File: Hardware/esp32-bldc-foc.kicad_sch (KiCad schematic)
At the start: 39 parts, among them J1 ENCODER, J2 I2C2, J3 VDRIVE, J4 MOTOR, P1 PCB_Pin_Breakout, P10 PCB_Pin_Breakout, P11 PCB_Pin_Breakout, P12 PCB_Pin_Breakout, P13 PCB_Pin_Breakout, P14 PCB_Pin_Breakout, P15 PCB_Pin_Breakout, P16 PCB_Pin_Breakout, P17 PCB_Pin_Breakout, P18 PCB_Pin_Breakout, P19 PCB_Pin_Breakout, P2 PCB_Pin_Breakout, P20 PCB_Pin_Breakout, P21 PCB_Pin_Breakout, P3 PCB_Pin_Breakout, P4 PCB_Pin_Breakout, P5 PCB_Pin_Breakout, P6 PCB_Pin_Breakout, P7 PCB_Pin_Breakout, P8 PCB_Pin_Breakout, P9 PCB_Pin_Breakout, U1 ESP32-S3-WROOM-1, U3 SRV05-4, U6 EG2133

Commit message: Pretty much all components now have values
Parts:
- added C16: 10u, symbol Device:C_Small
- C1: value C -> 10u
- C13, C2: value C -> 100n
- C3: value C -> 1u
- L1: value L -> BLM21
- R1, R3: value R -> 10k
- R5: value R_Small -> 10R
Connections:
- new net GND2: C16.1
- new net Vdrive: C16.2
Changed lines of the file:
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@@
 	(wire
 		(pts
+			(xy 49.53 167.64) (xy 49.53 170.18)
+		)
+		(stroke
+			(width 0)
+			(type default)
+		)
+	)
+	(wire
+		(pts
 			(xy 29.21 152.4) (xy 29.21 140.97)
 		)
@@
 	(wire
 		(pts
+			(xy 49.53 175.26) (xy 49.53 177.8)
+		)
+		(stroke
+			(width 0)
+			(type default)
+		)
+	)
+	(wire
+		(pts
 			(xy 87.63 134.62) (xy 90.17 134.62)
 		)
@@
 			)
 		)
-		(property "Value" "C"
+		(property "Value" "1u"
 			(at 232.791 138.3721 0)
 			(effects
@@
 			)
 		)
-		(property "Value" "C"
+		(property "Value" "100n"
 			(at 21.209 145.9921 0)
 			(effects
@@
 	)
 	(symbol
+		(lib_id "power:Vdrive")
+		(at 49.53 167.64 0)
+		(unit 1)
+		(exclude_from_sim no)
+		(in_bom yes)
+		(on_board yes)
+		(dnp no)
+		(fields_autoplaced yes)
+		(property "Reference" "#PWR01"
+			(at 49.53 171.45 0)
+			(effects
+				(font
+					(size 1.27 1.27)
+				)
+				(hide yes)
+			)
+		)
+		(property "Value" "Vdrive"
+			(at 49.53 163.5069 0)
+			(effects
+				(font
+					(size 1.27 1.27)
+				)
+			)
+		)
+		(property "Footprint" ""
+			(at 49.53 167.64 0)
+			(effects
+				(font
+					(size 1.27 1.27)
+				)
+				(hide yes)
+			)
+		)
+		(property "Datasheet" ""
+			(at 49.53 167.64 0)
+			(effects
+				(font
+					(size 1.27 1.27)
+				)
+				(hide yes)
+			)
+		)
+		(property "Description" "Power symbol creates a global label with name \"Vdrive\""
+			(at 49.53 167.64 0)
+			(effects
+				(font
+					(size 1.27 1.27)
+				)
+				(hide yes)
+			)
+		)
+		(pin "1"
+		)
+		(instances
+			(project "esp32-bldc-foc"
+				(path "/5fd9cc58-24f5-445f-b12c-0418263ff67c"
+					(reference "#PWR01")
+					(unit 1)
+				)
+			)
+		)
+	)
+	(symbol
 		(lib_id "power:+5V")
 		(at 168.91 125.73 0)
@@
 			)
 		)
-		(property "Value" "L"
+		(property "Value" "BLM21"
 			(at 55.2449 81.2221 0)
 			(effects
@@
 			)
 		)
-		(property "Value" "R"
+		(property "Value" "10k"
 			(at 267.208 125.6721 0)
 			(effects
@@
 			)
 		)
-		(property "Value" "R_Small"
+		(property "Value" "10R"
 			(at 56.1086 72.3321 0)
 			(effects
@@
 			)
 		)
-		(property "Value" "R"
+		(property "Value" "10k"
 			(at 231.648 125.6721 0)
 			(effects
@@
 	)
 	(symbol
+		(lib_id "Device:C_Small")
+		(at 49.53 172.72 180)
+		(unit 1)
+		(exclude_from_sim no)
+		(in_bom yes)
+		(on_board yes)
+		(dnp no)
+		(fields_autoplaced yes)
+		(property "Reference" "C16"
+			(at 51.8541 171.5014 0)
+			(effects
+				(font
+					(size 1.27 1.27)
+				)
+				(justify right)
+			)
+		)
+		(property "Value" "10u"
+			(at 51.8541 173.9257 0)
+			(effects
+				(font
+					(size 1.27 1.27)
+				)
+				(justify right)
+			)
+		)
+		(property "Footprint" ""
+			(at 49.53 172.72 0)
+			(effects
+				(font
+					(size 1.27 1.27)
+				)
+				(hide yes)
+			)
+		)
+		(property "Datasheet" "~"
+			(at 49.53 172.72 0)
+			(effects
+				(font
+					(size 1.27 1.27)
+				)
+				(hide yes)
+			)
+		)
+		(property "Description" "Unpolarized capacitor, small symbol"
+			(at 49.53 172.72 0)
+			(effects
+				(font
+					(size 1.27 1.27)
+				)
+				(hide yes)
+			)
+		)
+		(pin "1"
+		)
+		(pin "2"
+		)
+		(instances
+			(project "esp32-bldc-foc"
+				(path "/5fd9cc58-24f5-445f-b12c-0418263ff67c"
+					(reference "C16")
+					(unit 1)
+				)
+			)
+		)
+	)
+	(symbol
 		(lib_id "Device:C")
 		(at 142.24 31.75 0)
@@
 			)
 		)
-		(property "Value" "C"
+		(property "Value" "10u"
 			(at 139.319 32.9621 0)
 			(effects
@@
 			)
 		)
-		(property "Value" "C"
+		(property "Value" "100n"
 			(at 151.511 32.9621 0)
 			(effects
@@
 					(unit 1)
 				)
+			)
+		)
+	)
+	(symbol
+		(lib_id "power:GND2")
+		(at 49.53 177.8 0)
+		(unit 1)
+		(exclude_from_sim no)
+		(in_bom yes)
+		(on_board yes)
+		(dnp no)
+		(fields_autoplaced yes)
+		(property "Reference" "#PWR02"
+			(at 49.53 184.15 0)
+			(effects
+				(font
+					(size 1.27 1.27)
+				)
+				(hide yes)
+			)
+		)
+		(property "Value" "GND2"
+			(at 49.53 181.9331 0)
+			(effects
+				(font
+					(size 1.27 1.27)
+				)
+			)
+		)
+		(property "Footprint" ""
+			(at 49.53 177.8 0)
+			(effects
+				(font
+					(size 1.27 1.27)
+				)
+				(hide yes)
+			)
+		)
+		(property "Datasheet" ""
+			(at 49.53 177.8 0)
+			(effects
+				(font
+					(size 1.27 1.27)
+				)
+				(hide yes)
+			)
+		)
+		(property "Description" "Power symbol creates a global label with name \"GND2\" , ground"
+			(at 49.53 177.8 0)
+			(effects
+				(font
+					(size 1.27 1.27)
+				)
+				(hide yes)
+			)
+		)
+		(pin "1"
+		)
+		(instances
+			(project "esp32-bldc-foc"
+				(path "/5fd9cc58-24f5-445f-b12c-0418263ff67c"
+					(reference "#PWR02")
+					(unit 1)
+				)

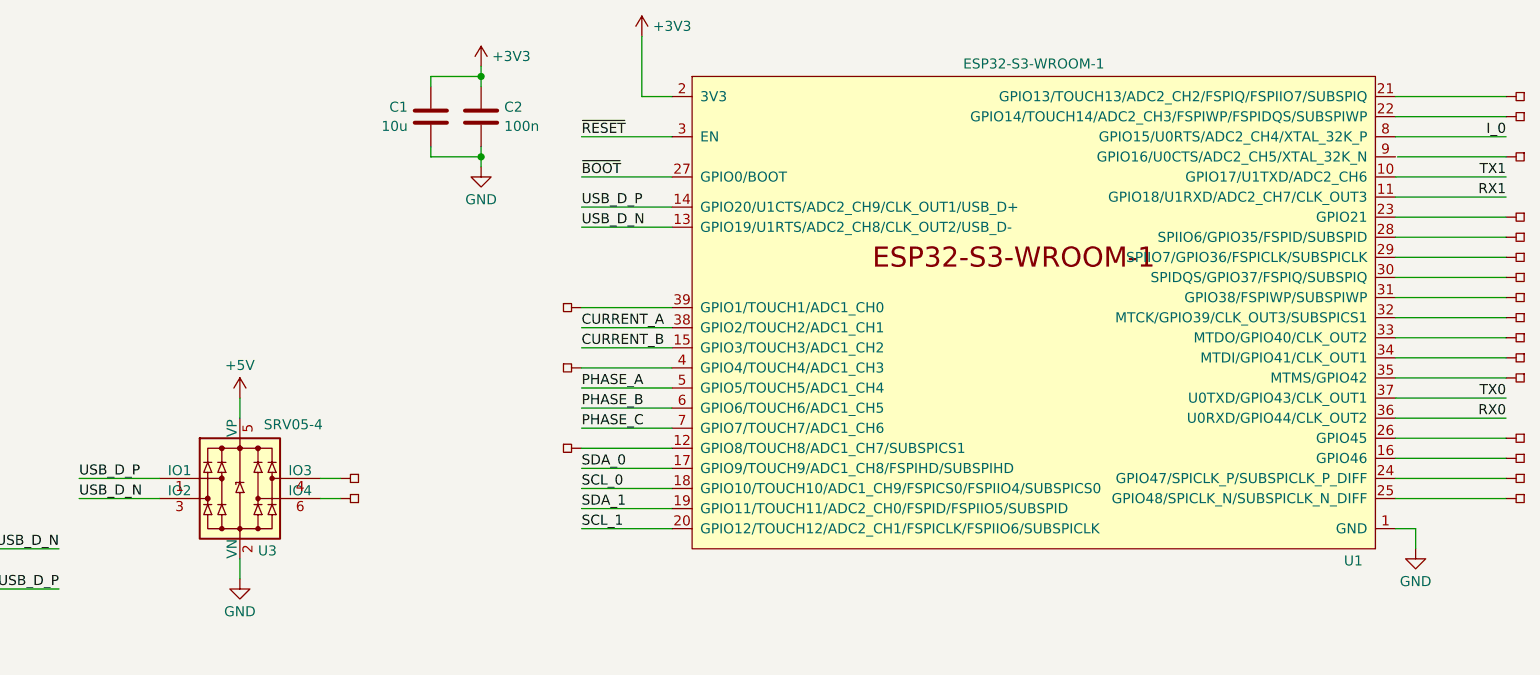
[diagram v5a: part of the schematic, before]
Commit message: Add jumpers to ESP32-S3
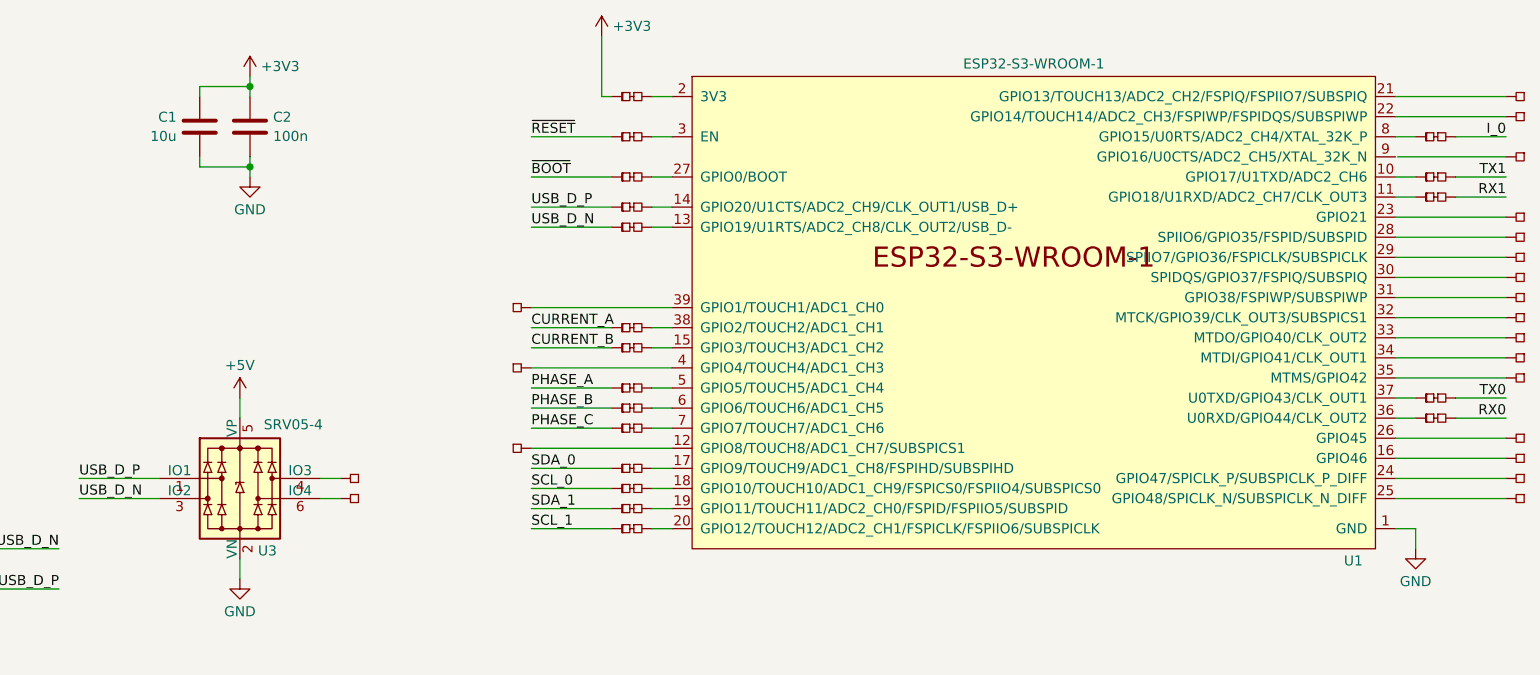
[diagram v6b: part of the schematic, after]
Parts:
- added P22, P23, P24, P25, P26, P27, P28, P29, P30, P31, P32, P33, P34, P35, P36, P37, P38, P39, P40: PCB_Patch, afork-kicad-parts:tinySJ-Bridged, symbol afork-kicad-parts:PCB_Patch
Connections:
- net +3V3: now also P40.1; no longer U1.2 (3V3)
- net CURRENT_A: now also P26.1; no longer U1.38 (GPIO2/TOUCH2/ADC1_CH1)
- net CURRENT_B: now also P27.1; no longer U1.15 (GPIO3/TOUCH3/ADC1_CH2)
- net I_0: now also P35.2; no longer U1.8 (GPIO15/U0RTS/ADC2_CH4/XTAL_32K_P)
- net PHASE_A: now also P28.1; no longer U1.5 (GPIO5/TOUCH5/ADC1_CH4)
- net PHASE_B: now also P29.1; no longer U1.6 (GPIO6/TOUCH6/ADC1_CH5)
- net PHASE_C: now also P30.1; no longer U1.7 (GPIO7/TOUCH7/ADC1_CH6)
- net RX0: now also P39.2; no longer U1.36 (U0RXD/GPIO44/CLK_OUT2)
- net RX1: now also P37.2; no longer U1.11 (GPIO18/U1RXD/ADC2_CH7/CLK_OUT3)
- net SCL_0: now also P32.1; no longer U1.18 (GPIO10/TOUCH10/ADC1_CH9/FSPICS0/FSPIIO4/SUBSPICS0)
- net SCL_1: now also P34.1; no longer U1.20 (GPIO12/TOUCH12/ADC2_CH1/FSPICLK/FSPIIO6/SUBSPICLK)
- net SDA_0: now also P31.1; no longer U1.17 (GPIO9/TOUCH9/ADC1_CH8/FSPIHD/SUBSPIHD)
- net SDA_1: now also P33.1; no longer U1.19 (GPIO11/TOUCH11/ADC2_CH0/FSPID/FSPIIO5/SUBSPID)
- net TX0: now also P38.2; no longer U1.37 (U0TXD/GPIO43/CLK_OUT1)
- net TX1: now also P36.2; no longer U1.10 (GPIO17/U1TXD/ADC2_CH6)
- net USB_D_N: now also P25.1; no longer U1.13 (GPIO19/U1RTS/ADC2_CH8/CLK_OUT2/USB_D-)
- net USB_D_P: now also P24.1; no longer U1.14 (GPIO20/U1CTS/ADC2_CH9/CLK_OUT1/USB_D+)
- net ~{BOOT}: now also P23.1; no longer U1.27 (GPIO0/BOOT)
- net ~{RESET}: now also P22.1; no longer U1.3 (EN)
- new net: P30.2, U1.7 (GPIO7/TOUCH7/ADC1_CH6)
- new net: P26.2, U1.38 (GPIO2/TOUCH2/ADC1_CH1)
- new net: P24.2, U1.14 (GPIO20/U1CTS/ADC2_CH9/CLK_OUT1/USB_D+)
- new net: P36.1, U1.10 (GPIO17/U1TXD/ADC2_CH6)
- new net: P23.2, U1.27 (GPIO0/BOOT)
- new net: P29.2, U1.6 (GPIO6/TOUCH6/ADC1_CH5)
- new net: P35.1, U1.8 (GPIO15/U0RTS/ADC2_CH4/XTAL_32K_P)
- new net: P37.1, U1.11 (GPIO18/U1RXD/ADC2_CH7/CLK_OUT3)
- new net: P27.2, U1.15 (GPIO3/TOUCH3/ADC1_CH2)
- new net: P34.2, U1.20 (GPIO12/TOUCH12/ADC2_CH1/FSPICLK/FSPIIO6/SUBSPICLK)
- new net: P28.2, U1.5 (GPIO5/TOUCH5/ADC1_CH4)
- new net: P39.1, U1.36 (U0RXD/GPIO44/CLK_OUT2)
- new net: P32.2, U1.18 (GPIO10/TOUCH10/ADC1_CH9/FSPICS0/FSPIIO4/SUBSPICS0)
- new net: P22.2, U1.3 (EN)
- new net: P40.2, U1.2 (3V3)
- new net: P25.2, U1.13 (GPIO19/U1RTS/ADC2_CH8/CLK_OUT2/USB_D-)
- new net: P31.2, U1.17 (GPIO9/TOUCH9/ADC1_CH8/FSPIHD/SUBSPIHD)
- new net: P33.2, U1.19 (GPIO11/TOUCH11/ADC2_CH0/FSPID/FSPIIO5/SUBSPID)
- new net: P38.1, U1.37 (U0TXD/GPIO43/CLK_OUT1)
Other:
- moved on the sheet: C1, C2

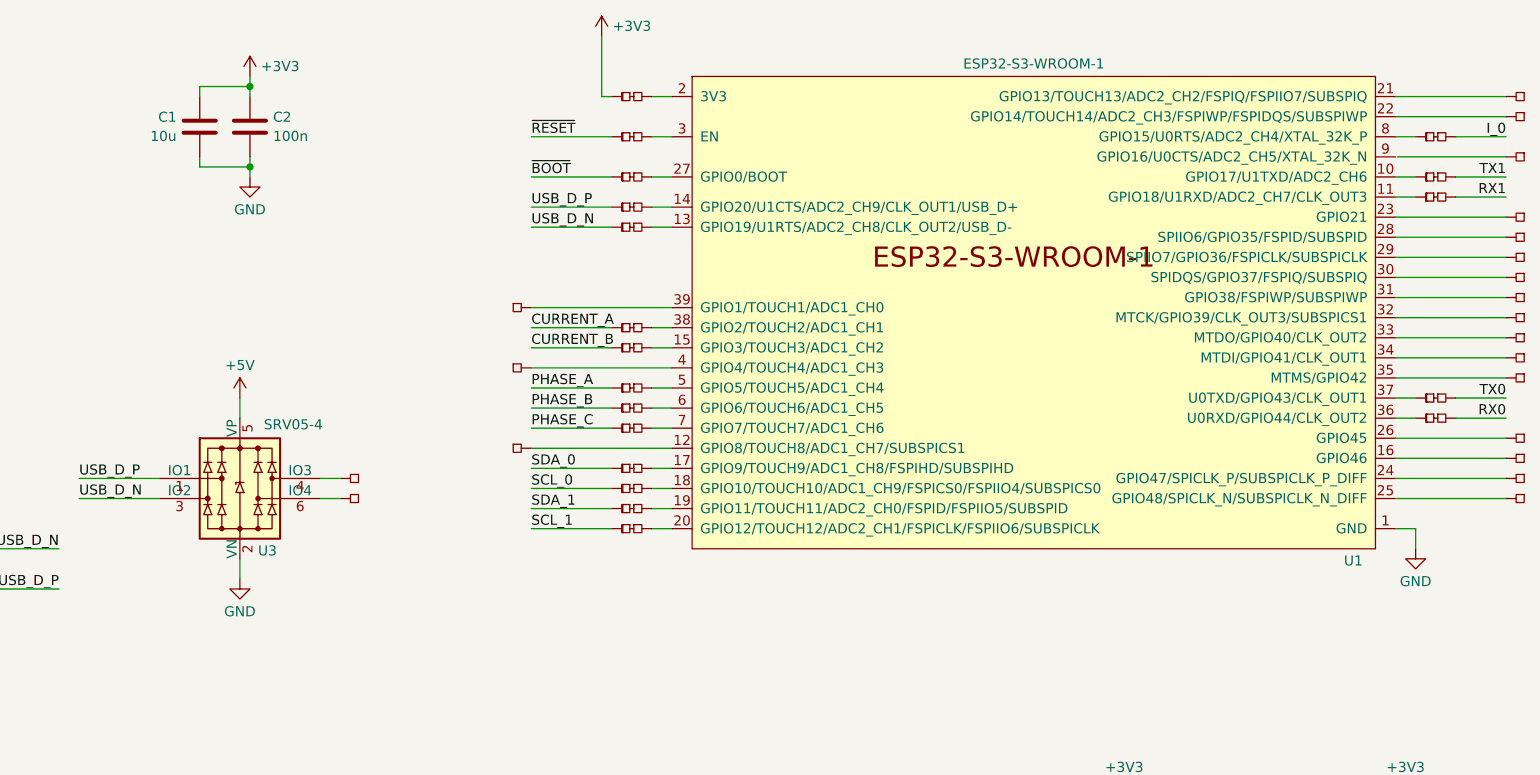
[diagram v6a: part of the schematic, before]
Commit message: First cut of PCB (early parts)
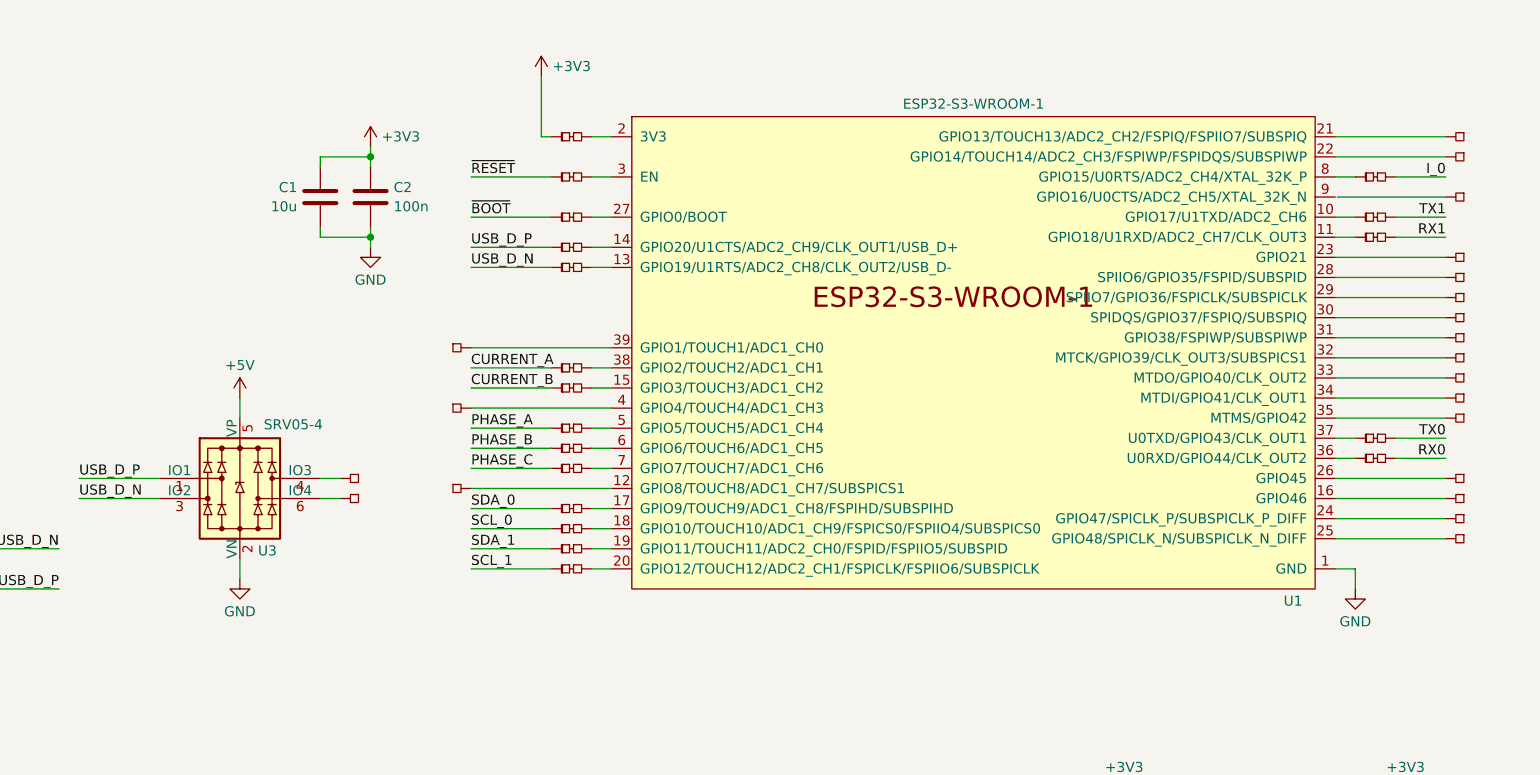
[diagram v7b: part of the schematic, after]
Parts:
- J2: footprint Connector_PinHeader_2.54mm:PinHeader_1x04_P2.54mm_Vertical -> Connector_JST:JST_SH_SM04B-SRSS-TB_1x04-1MP_P1.00mm_Horizontal
- U1: footprint Espressif:ESP32-S3-WROOM-1 -> RF_Module:ESP32-S3-WROOM-1
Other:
- moved on the sheet: C1, C2, U1
